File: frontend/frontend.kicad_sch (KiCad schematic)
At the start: 60 parts, among them Q1 T2N7002AK,LM, Q2 NX3008PBK,215, Q3 NX3008PBK,215, Q4 T2N7002AK,LM, Q5 NX3008PBK,215, Q6 T2N7002AK,LM, U1 ADS1291/2, U2 KC2016Z2

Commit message: Tweak frontend
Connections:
- net L: now reaches ECG1.1, Q5.1 (G), R1.1, R3.1
- net L: now also R7.2
- net LL: now reaches ECG4.1, R6.1
- net R: now reaches ECG2.1, R12.2, R2.1
- net L2: now reaches ECG3.1, R5.1
- net L2: now also R7.1
- net ECG1N: no longer names the net of C11.1, C17.1, R1.2, U1.3 (IN1N)
- net ECG1N: no longer R7.1
- net ECG1P: no longer names the net of C12.1, C17.2, R2.2, U1.4 (IN1P)
- net ECG2N: no longer names the net of C13.1, C15.1, R5.2, U1.5 (IN2N)
- net ECG2N: no longer R7.2
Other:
- note added: "Lead I: ECG2 - ECG1 Lead II: ECG4 - ECG2 Lead III: ECG4 - ECG1"
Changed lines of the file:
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@@
   (title_block
     (title "Card/IO ECG daughter board")
-    (date "2023-10-07")
+    (date "2023-11-04")
     (rev "5")
   )
@@
     (effects (font (size 1.27 1.27)) (justify left bottom))
   )
+  (text "Lead I: ECG2 - ECG1\nLead II: ECG4 - ECG2\nLead III: ECG4 - ECG1"
+    (at -17.78 142.24 0)
+    (effects (font (size 1.27 1.27)) (justify left bottom))
+  )
   (text "Switched pulldown" (at 25.4 129.54 0)
     (effects (font (size 1.27 1.27)) (justify left bottom))
@@
     (effects (font (size 1.27 1.27)) (justify right bottom))
   )
-  (label "ECG2N" (at 82.55 180.34 0) (fields_autoplaced)
+  (label "ECG2P" (at 88.9 109.22 180) (fields_autoplaced)
+    (effects (font (size 1.27 1.27)) (justify right bottom))
+  )
+  (label "L" (at 82.55 180.34 0) (fields_autoplaced)
     (effects (font (size 1.27 1.27)) (justify left bottom))
   )
@@
     (effects (font (size 1.27 1.27)) (justify right bottom))
   )
-  (label "ECG1P" (at 78.74 101.6 0) (fields_autoplaced)
-    (effects (font (size 1.27 1.27)) (justify left bottom))
-  )
-  (label "ECG1N" (at 78.74 99.06 0) (fields_autoplaced)
-    (effects (font (size 1.27 1.27)) (justify left bottom))
-  )
-  (label "ECG2P" (at 78.74 109.22 0) (fields_autoplaced)
-    (effects (font (size 1.27 1.27)) (justify left bottom))
-  )
   (label "TOUCH_OFF" (at 85.09 35.56 180) (fields_autoplaced)
     (effects (font (size 1.27 1.27)) (justify right bottom))
@@
     (effects (font (size 1.27 1.27)) (justify left bottom))
   )
+  (label "L" (at 25.4 93.98 0) (fields_autoplaced)
+    (effects (font (size 1.27 1.27)) (justify left bottom))
+  )
+  (label "R" (at 25.4 111.76 0) (fields_autoplaced)
+    (effects (font (size 1.27 1.27)) (justify left bottom))
+  )
   (label "TOFF" (at 59.69 30.48 0) (fields_autoplaced)
     (effects (font (size 1.27 1.27)) (justify left bottom))
   )
-  (label "ECG2N" (at 78.74 106.68 0) (fields_autoplaced)
-    (effects (font (size 1.27 1.27)) (justify left bottom))
-  )
-  (label "ECG1N" (at 74.93 180.34 180) (fields_autoplaced)
+  (label "L2" (at 25.4 158.75 0) (fields_autoplaced)
+    (effects (font (size 1.27 1.27)) (justify left bottom))
+  )
+  (label "LL" (at 25.4 176.53 0) (fields_autoplaced)
+    (effects (font (size 1.27 1.27)) (justify left bottom))
+  )
+  (label "L2" (at 74.93 180.34 180) (fields_autoplaced)
     (effects (font (size 1.27 1.27)) (justify right bottom))
   )

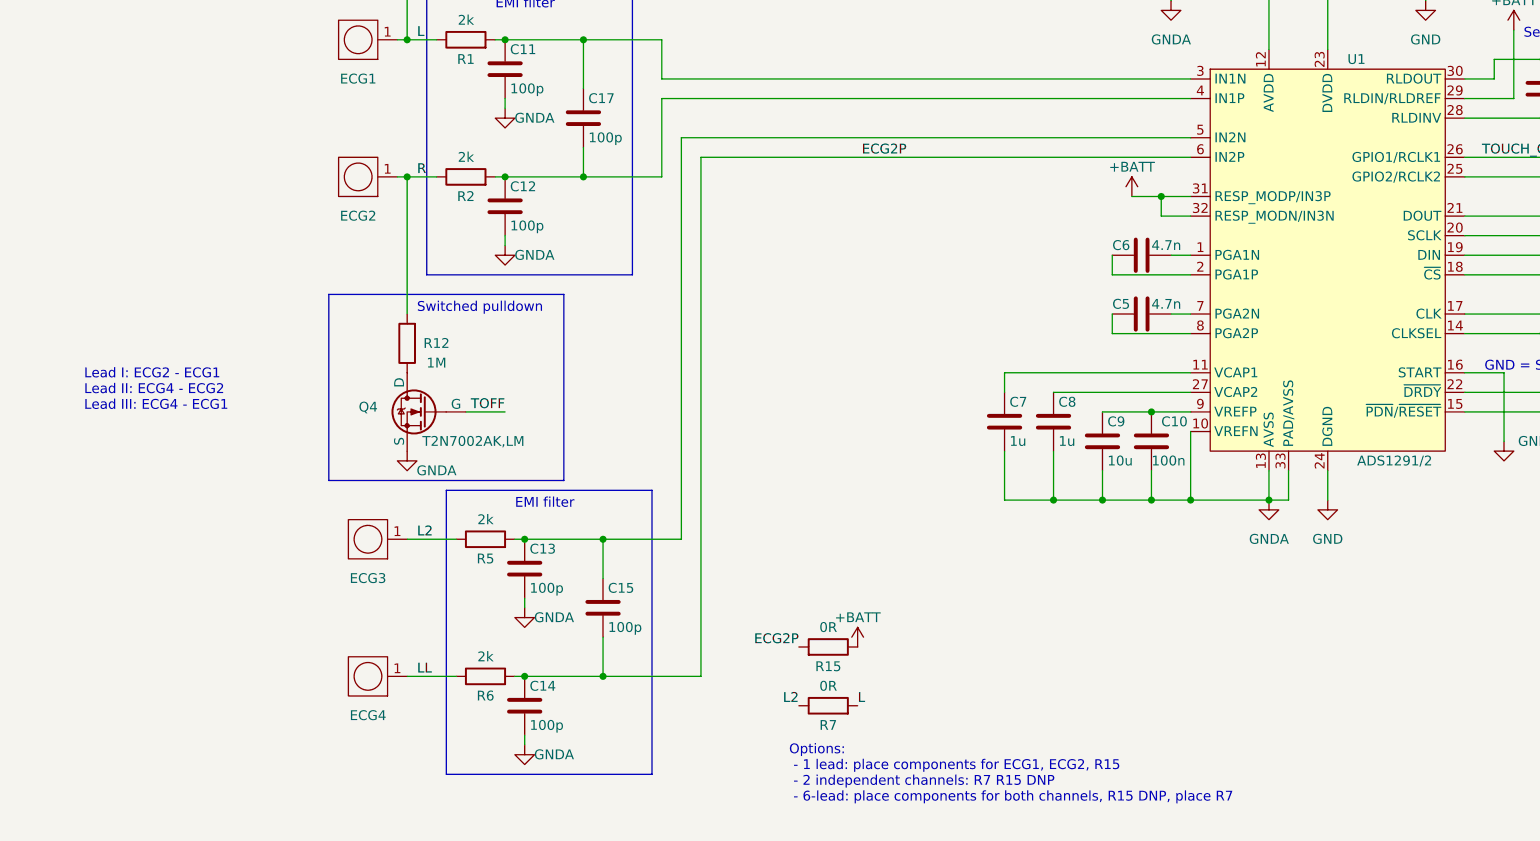
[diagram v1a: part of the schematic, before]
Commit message: Final tweaks: switch ch2 electrodes
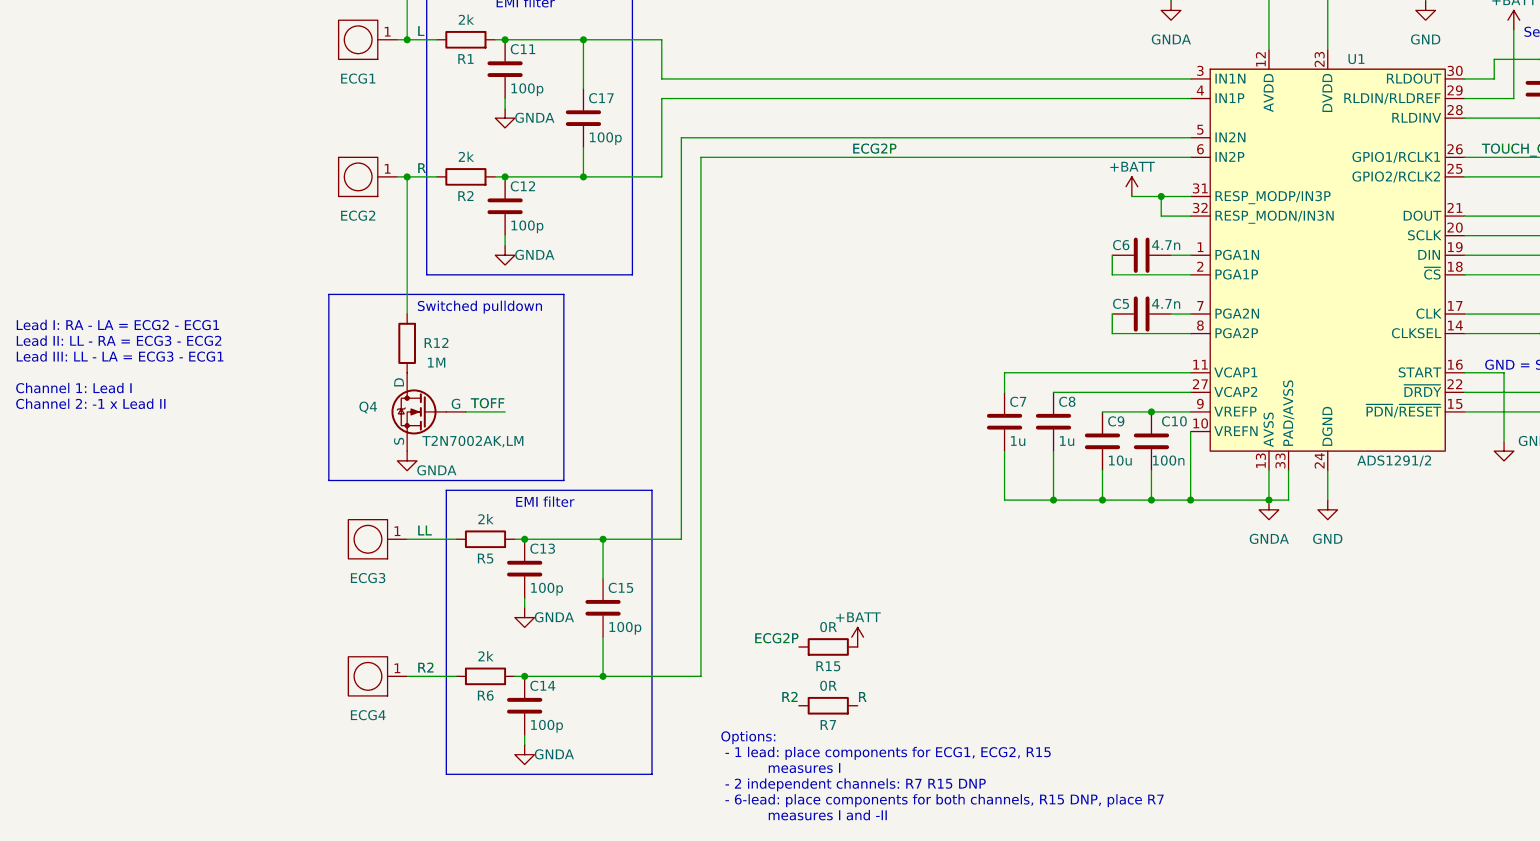
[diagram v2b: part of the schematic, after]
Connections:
- net L: no longer R7.2
- net LL: now also ECG3.1, R5.1; no longer ECG4.1, R6.1
- net R: now also R7.2
- removed net L2: ECG3.1, R5.1, R7.1
- new net R2: ECG4.1, R6.1, R7.1
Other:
- note added: "Lead I: RA - LA = ECG2 - ECG1 Lead II: LL - RA = ECG3 - ECG2 Lead III: LL - LA = ECG3 - ECG1 Channel 1: Lead I Channel 2: -1 x Lead II"
- note added: "Options: - 1 lead: place components for ECG1, ECG2, R15 measures I - 2 independent channels: R7 R15 DNP - 6-lead: place components for both channels, R15 DNP, place R7 measures I and -II"
- note removed: "Lead I: ECG2 - ECG1 Lead II: ECG4 - ECG2 Lead III: ECG4 - ECG1"
- note removed: "Options: - 1 lead: place components for ECG1, ECG2, R15 - 2 independent channels: R7 R15 DNP - 6-lead: place components for both channels, R15 DNP, place R7"
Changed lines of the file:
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@@
+    (stroke (width 0) (type default))
+  )
+  (wire (pts (xy 59.69 106.68) (xy 125.73 106.68))
     (stroke (width 0) (type default))
   )
@@
   )
   (wire (pts (xy 125.73 144.78) (xy 125.73 153.67))
-    (stroke (width 0) (type default))
-  )
-  (wire (pts (xy 59.69 106.68) (xy 125.73 106.68))
     (stroke (width 0) (type default))
   )
@@
     (effects (font (size 1.27 1.27)) (justify left bottom))
   )
-  (text "Options:\n - 1 lead: place components for ECG1, ECG2, R15\n - 2 independent channels: R7 R15 DNP\n - 6-lead: place components for both channels, R15 DNP, place R7"
-    (at 73.66 193.04 0)
+  (text "Options:\n - 1 lead: place components for ECG1, ECG2, R15\n           measures I\n - 2 independent channels: R7 R15 DNP\n - 6-lead: place components for both channels, R15 DNP, place R7\n           measures I and -II"
+    (at 64.77 195.58 0)
     (effects (font (size 1.27 1.27)) (justify left bottom))
   )
-  (text "Lead I: ECG2 - ECG1\nLead II: ECG4 - ECG2\nLead III: ECG4 - ECG1"
-    (at -17.78 142.24 0)
+  (text "Lead I: RA - LA = ECG2 - ECG1\nLead II: LL - RA = ECG3 - ECG2\nLead III: LL - LA = ECG3 - ECG1\n\nChannel 1: Lead I\nChannel 2: -1 x Lead II"
+    (at -26.67 142.24 0)
     (effects (font (size 1.27 1.27)) (justify left bottom))
   )
@@
     (effects (font (size 1.27 1.27)) (justify right bottom))
   )
-  (label "ECG2P" (at 88.9 109.22 180) (fields_autoplaced)
+  (label "ECG2P" (at 87.63 109.22 180) (fields_autoplaced)
     (effects (font (size 1.27 1.27)) (justify right bottom))
   )
-  (label "L" (at 82.55 180.34 0) (fields_autoplaced)
+  (label "R" (at 82.55 180.34 0) (fields_autoplaced)
     (effects (font (size 1.27 1.27)) (justify left bottom))
   )
@@
     (effects (font (size 1.27 1.27)) (justify left bottom))
   )
-  (label "L2" (at 25.4 158.75 0) (fields_autoplaced)
+  (label "R2" (at 25.4 176.53 0) (fields_autoplaced)
     (effects (font (size 1.27 1.27)) (justify left bottom))
   )
-  (label "LL" (at 25.4 176.53 0) (fields_autoplaced)
+  (label "LL" (at 25.4 158.75 0) (fields_autoplaced)
     (effects (font (size 1.27 1.27)) (justify left bottom))
   )
-  (label "L2" (at 74.93 180.34 180) (fields_autoplaced)
+  (label "R2" (at 74.93 180.34 180) (fields_autoplaced)
     (effects (font (size 1.27 1.27)) (justify right bottom))
   )

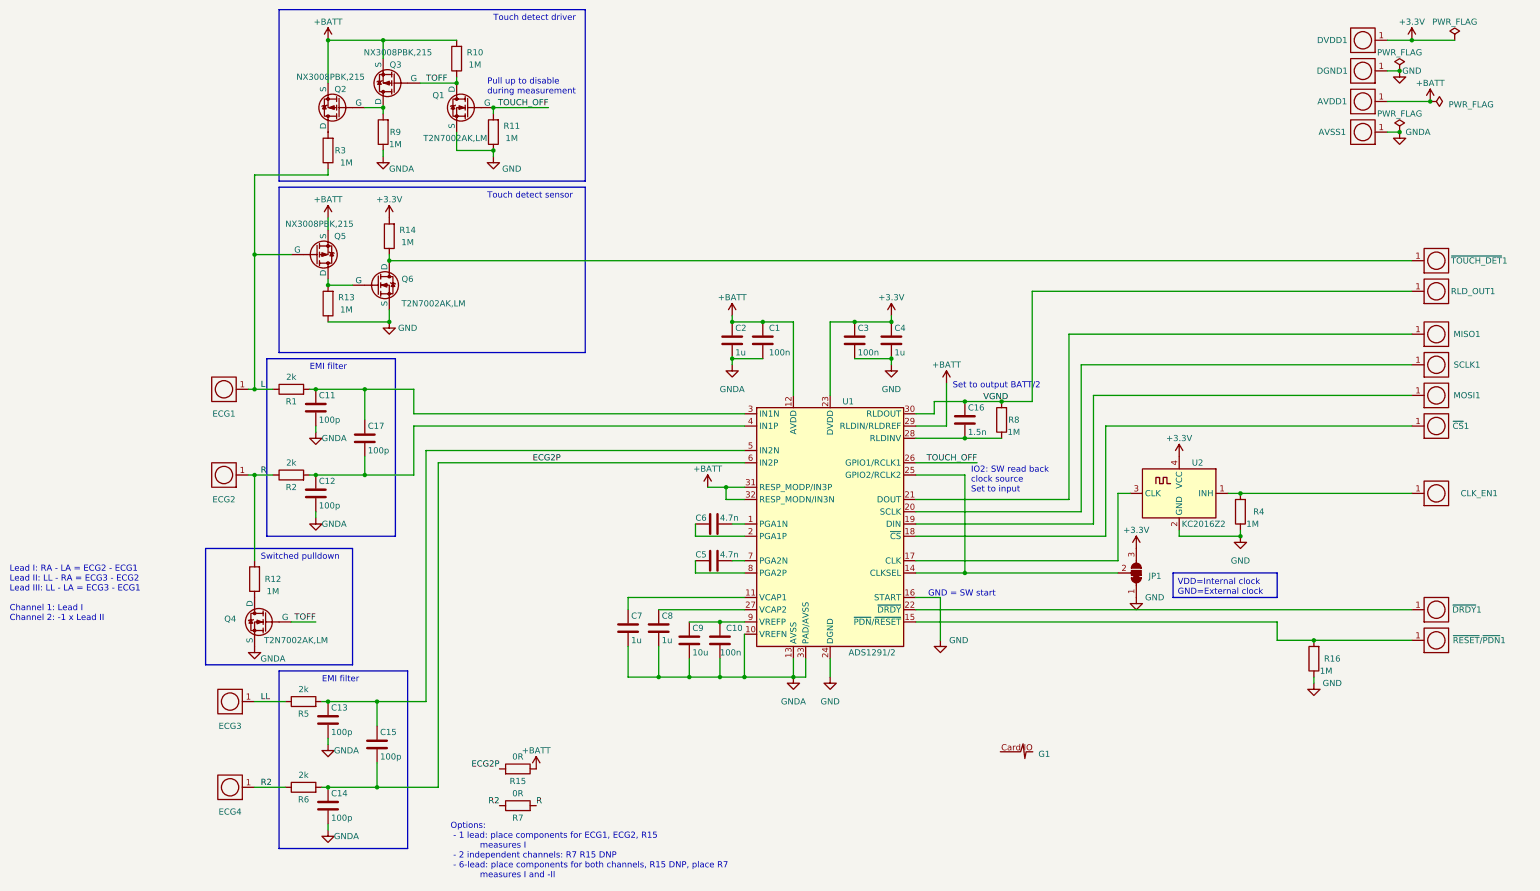
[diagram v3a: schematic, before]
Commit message: r8: fix main board issues, update frontend clksel
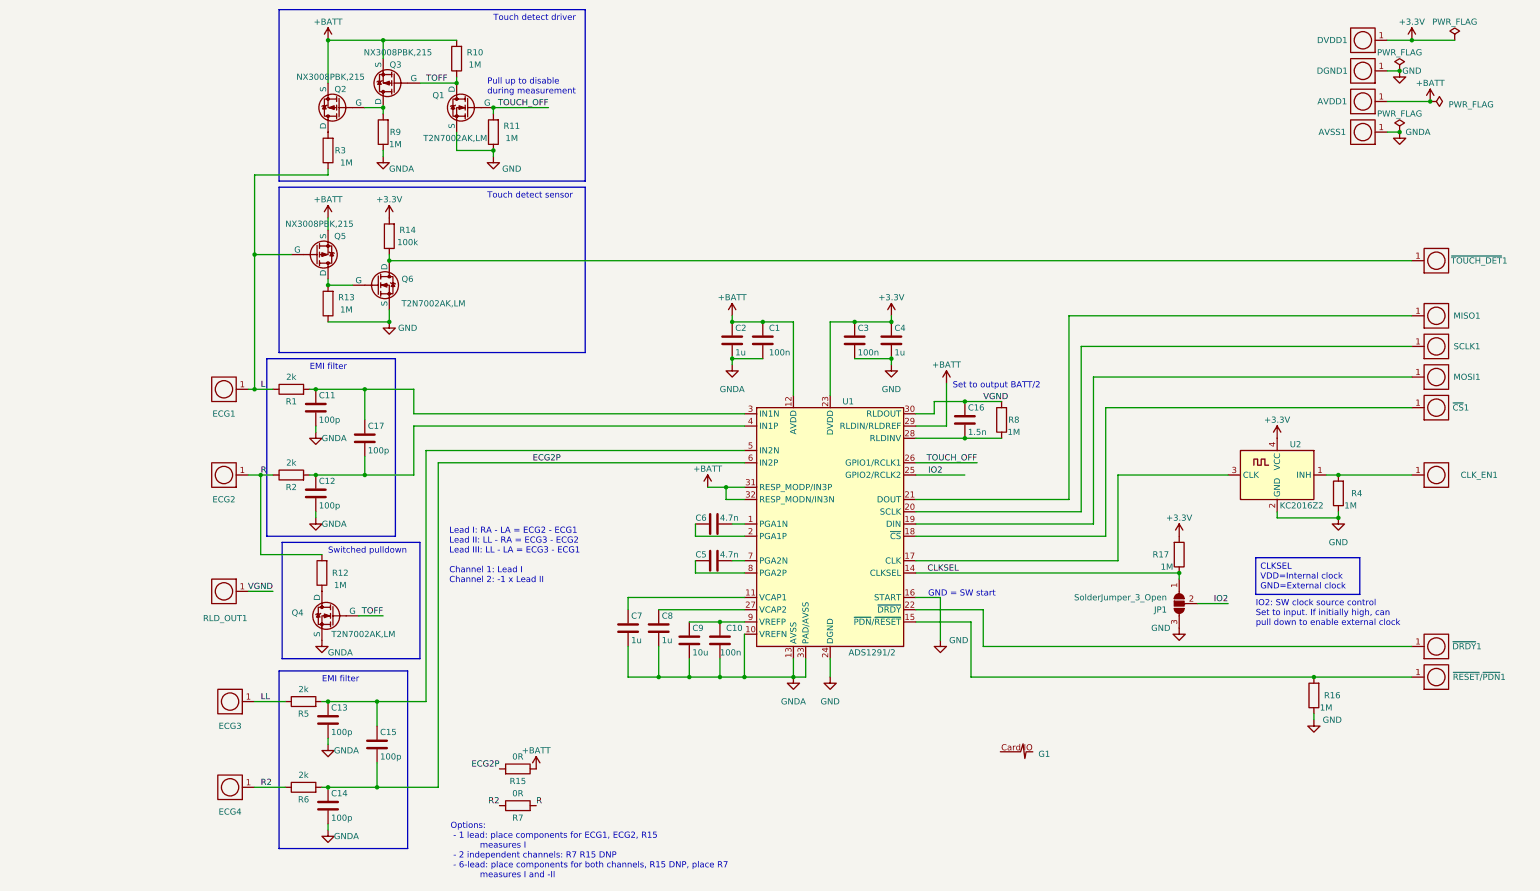
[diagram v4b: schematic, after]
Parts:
- removed JP1: SolderJumper_3_Bridged12, Jumper:SolderJumper-3_P1.3mm_Bridged12_RoundedPad1.0x1.5mm, symbol Jumper:SolderJumper_3_Bridged12
- added JP1: SolderJumper_3_Open, Jumper:SolderJumper-3_P1.3mm_Open_RoundedPad1.0x1.5mm, symbol Jumper:SolderJumper_3_Open
- added R17: 1M, Resistor_SMD:R_0603_1608Metric, symbol Device:R
- R14: value 1M -> 100k
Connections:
- net +3.3V: now also R17.2
- net GND: now also JP1.3 (B)
- net CLKSEL: now reaches U1.14 (CLKSEL)
- net CLKSEL: now also JP1.1 (A), R17.1; no longer U1.25 (GPIO2/RCLK2)
- new net IO2: JP1.2 (C), U1.25 (GPIO2/RCLK2)
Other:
- note added: "IO2: SW clock source control Set to input. If initially high, can pull down to enable external clock"
- note removed: "IO2: SW read back clock source Set to input"
- moved on the sheet: CLK_EN1, MISO1, MOSI1, Q4, R12, R16, R4, RLD_OUT1, SCLK1, U2, ~{CS}1, ~{DRDY}1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
